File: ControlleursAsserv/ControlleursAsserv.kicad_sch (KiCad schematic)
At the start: 42 parts, among them J1 I2C1_5, J2 I2C2_5, J3 CAN1, J4 CAN2, J5 In App Prog, J6 DEBUG, SW1 RESET, SW2 BOOT0, U1 STM32G474RETx, U2 AMS1117-3.3, U3 MCP2558FD-xSN, Y1 16MHz

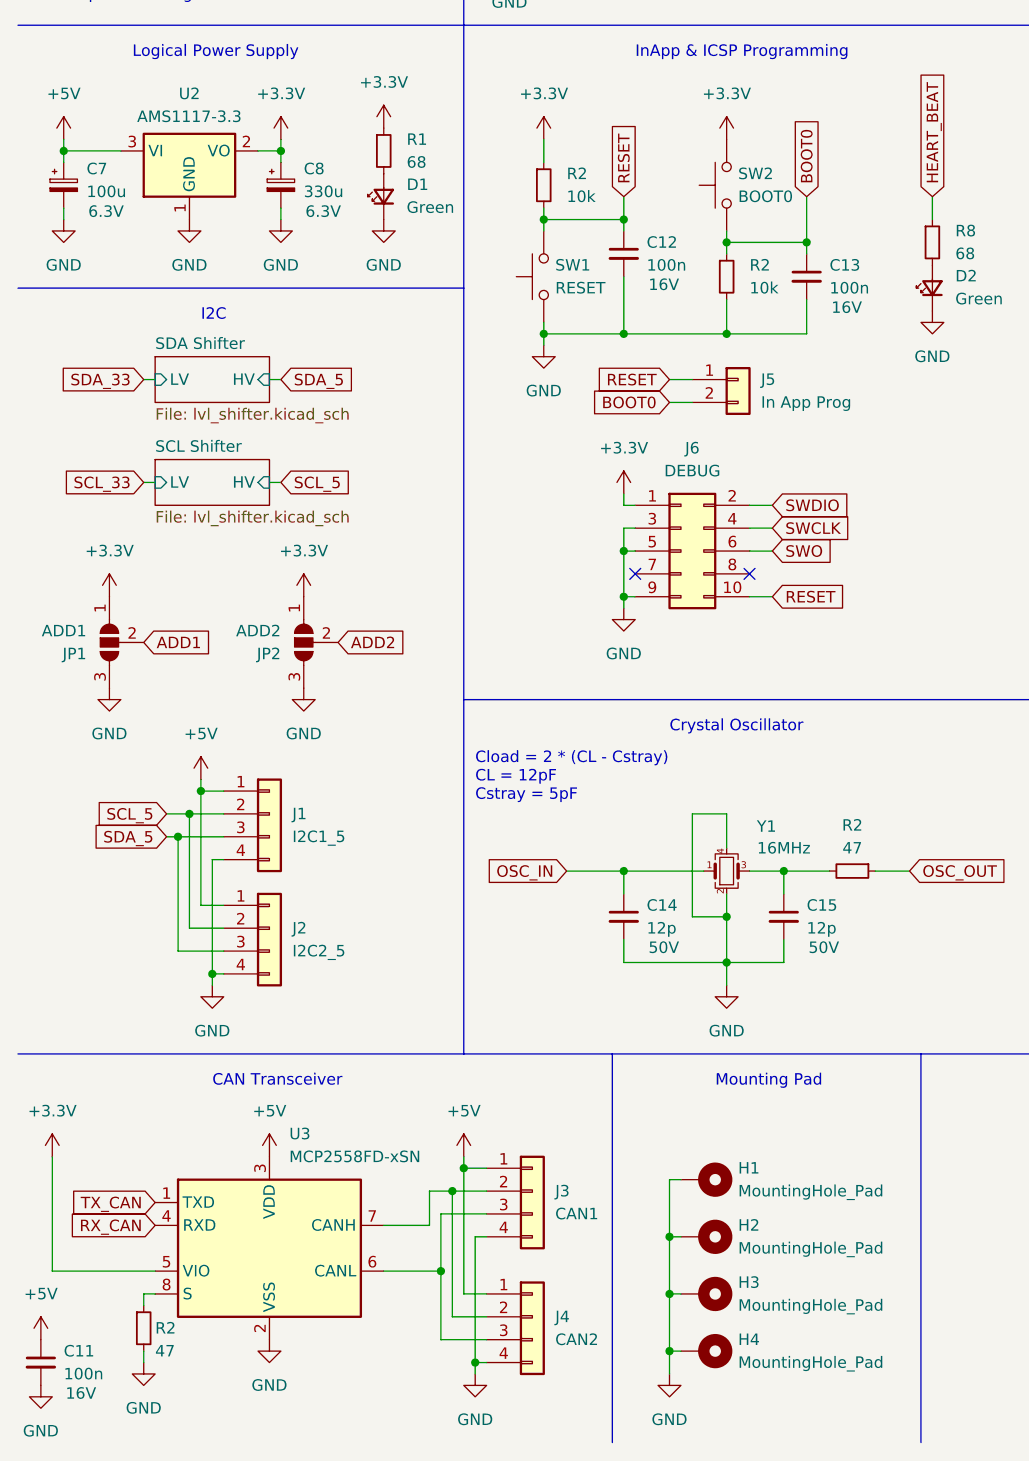
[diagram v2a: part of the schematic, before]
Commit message: Finalize placement for AsservController
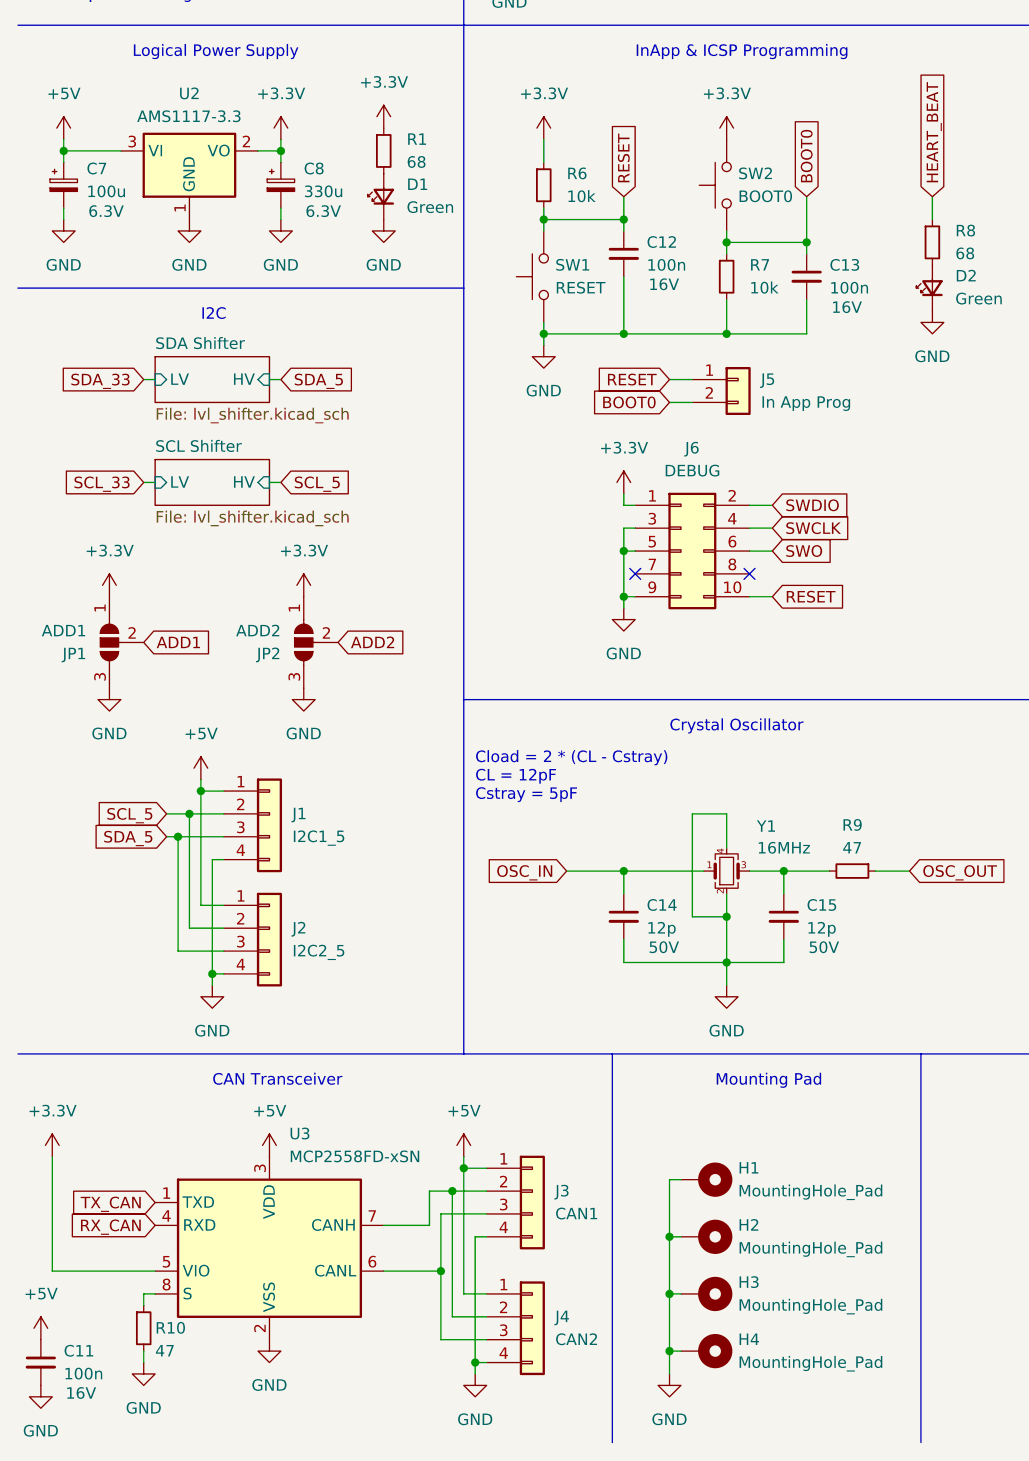
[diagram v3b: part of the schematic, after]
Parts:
- J1, J2, J3, J4: footprint Connector_JST:JST_EH_S4B-EH_1x04_P2.50mm_Horizontal -> Connector_JST:JST_PH_S4B-PH-K_1x04_P2.00mm_Horizontal
- J5: footprint Connector_JST:JST_EH_S2B-EH_1x02_P2.50mm_Horizontal -> Connector_JST:JST_PH_S2B-PH-K_1x02_P2.00mm_Horizontal
- renumbered R2 to R10, R2 to R6, R2 to R7, R2 to R9
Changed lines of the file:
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@@
       (effects (font (size 1.27 1.27)) (justify left))
     )
-    (property "Footprint" "Connector_JST:JST_EH_S4B-EH_1x04_P2.50mm_Horizontal" (at 69.85 168.91 0)
+    (property "Footprint" "Connector_JST:JST_PH_S4B-PH-K_1x04_P2.00mm_Horizontal" (at 69.85 168.91 0)
       (effects (font (size 1.27 1.27)) hide)
     )
@@
       (effects (font (size 1.27 1.27)) (justify left))
     )
-    (property "Footprint" "Connector_JST:JST_EH_S4B-EH_1x04_P2.50mm_Horizontal" (at 40.64 139.7 0)
+    (property "Footprint" "Connector_JST:JST_PH_S4B-PH-K_1x04_P2.00mm_Horizontal" (at 40.64 139.7 0)
       (effects (font (size 1.27 1.27)) hide)
     )
@@
       (effects (font (size 1.27 1.27)) (justify left))
     )
-    (property "Footprint" "Connector_JST:JST_EH_S4B-EH_1x04_P2.50mm_Horizontal" (at 69.85 182.88 0)
+    (property "Footprint" "Connector_JST:JST_PH_S4B-PH-K_1x04_P2.00mm_Horizontal" (at 69.85 182.88 0)
       (effects (font (size 1.27 1.27)) hide)
     )
@@
       (effects (font (size 1.27 1.27)) (justify left))
     )
-    (property "Footprint" "Connector_JST:JST_EH_S4B-EH_1x04_P2.50mm_Horizontal" (at 40.64 127 0)
+    (property "Footprint" "Connector_JST:JST_PH_S4B-PH-K_1x04_P2.00mm_Horizontal" (at 40.64 127 0)
       (effects (font (size 1.27 1.27)) hide)
     )
@@
   (symbol (lib_id "Device:R_Small") (at 91.44 67.31 0) (unit 1)
     (in_bom yes) (on_board yes) (dnp no) (fields_autoplaced)
-    (property "Reference" "R2" (at 93.98 66.04 0)
+    (property "Reference" "R7" (at 93.98 66.04 0)
       (effects (font (size 1.27 1.27)) (justify left))
     )
@@
     (instances
       (project "ControlleursAsserv"
-        (path "/c83bc042-587c-48f9-abdb-41233c8ec938/3da43f86-0520-4797-8d8a-f370cac20cce"
-          (reference "R2") (unit 1)
-        )
-        (path "/c83bc042-587c-48f9-abdb-41233c8ec938/089105fe-c96c-467a-9c54-c49136cd48fd"
-          (reference "R4") (unit 1)
-        )
         (path "/c83bc042-587c-48f9-abdb-41233c8ec938"
           (reference "R7") (unit 1)
@@
   (symbol (lib_id "Device:R_Small") (at 26.67 184.15 0) (unit 1)
     (in_bom yes) (on_board yes) (dnp no)
-    (property "Reference" "R2" (at 27.94 184.15 0)
+    (property "Reference" "R10" (at 27.94 184.15 0)
       (effects (font (size 1.27 1.27)) (justify left))
     )
@@
     (instances
       (project "ControlleursAsserv"
-        (path "/c83bc042-587c-48f9-abdb-41233c8ec938/3da43f86-0520-4797-8d8a-f370cac20cce"
-          (reference "R2") (unit 1)
-        )
-        (path "/c83bc042-587c-48f9-abdb-41233c8ec938/089105fe-c96c-467a-9c54-c49136cd48fd"
-          (reference "R4") (unit 1)
-        )
         (path "/c83bc042-587c-48f9-abdb-41233c8ec938"
           (reference "R10") (unit 1)
@@
   (symbol (lib_id "Device:R_Small") (at 71.12 57.15 0) (unit 1)
     (in_bom yes) (on_board yes) (dnp no) (fields_autoplaced)
-    (property "Reference" "R2" (at 73.66 55.88 0)
+    (property "Reference" "R6" (at 73.66 55.88 0)
       (effects (font (size 1.27 1.27)) (justify left))
     )
@@
     (instances
       (project "ControlleursAsserv"
-        (path "/c83bc042-587c-48f9-abdb-41233c8ec938/3da43f86-0520-4797-8d8a-f370cac20cce"
-          (reference "R2") (unit 1)
-        )
-        (path "/c83bc042-587c-48f9-abdb-41233c8ec938/089105fe-c96c-467a-9c54-c49136cd48fd"
-          (reference "R4") (unit 1)
-        )
         (path "/c83bc042-587c-48f9-abdb-41233c8ec938"
           (reference "R6") (unit 1)
@@
   (symbol (lib_id "Device:R_Small") (at 105.41 133.35 270) (unit 1)
     (in_bom yes) (on_board yes) (dnp no) (fields_autoplaced)
-    (property "Reference" "R2" (at 105.41 128.27 90)
+    (property "Reference" "R9" (at 105.41 128.27 90)
       (effects (font (size 1.27 1.27)))
     )
@@
     (instances
       (project "ControlleursAsserv"
-        (path "/c83bc042-587c-48f9-abdb-41233c8ec938/3da43f86-0520-4797-8d8a-f370cac20cce"
-          (reference "R2") (unit 1)
-        )
-        (path "/c83bc042-587c-48f9-abdb-41233c8ec938/089105fe-c96c-467a-9c54-c49136cd48fd"
-          (reference "R4") (unit 1)
-        )
         (path "/c83bc042-587c-48f9-abdb-41233c8ec938"
           (reference "R9") (unit 1)
@@
       (effects (font (size 1.27 1.27)) (justify left))
     )
-    (property "Footprint" "Connector_JST:JST_EH_S2B-EH_1x02_P2.50mm_Horizontal" (at 92.71 78.74 0)
-      (effects (font (size 1.27 1.27)) hide)
-    )
+    (property "Footprint" "Connector_JST:JST_PH_S2B-PH-K_1x02_P2.00mm_Horizontal" (at 92.71 78.74 0)
+      (effects (font (size 1.27 1.27)) hide)
+    )

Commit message: Init routing
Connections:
- net DIR_1: now also U1.4 (PC15); no longer U1.2 (PC13)
- net DIR_3: now also U1.2 (PC13); no longer U1.4 (PC15)
- net SLEEP_1: now also U1.22 (PC4); no longer U1.24 (PB0)
- net SLEEP_3: now also U1.24 (PB0); no longer U1.22 (PC4)
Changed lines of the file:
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@@
     )
   )
-  (global_label "SLEEP_3" (shape input) (at 213.36 83.82 180) (fields_autoplaced)
-    (effects (font (size 1.27 1.27)) (justify right))
-    (property "Intersheetrefs" "${INTERSHEET_REFS}" (at 202.3921 83.82 0)
-      (effects (font (size 1.27 1.27)) (justify right) hide)
+  (global_label "SLEEP_3" (shape input) (at 255.27 93.98 0) (fields_autoplaced)
+    (effects (font (size 1.27 1.27)) (justify left))
+    (property "Intersheetrefs" "${INTERSHEET_REFS}" (at 266.2379 93.98 0)
+      (effects (font (size 1.27 1.27)) (justify left) hide)
     )
   )
@@
     )
   )
-  (global_label "SLEEP_1" (shape input) (at 255.27 93.98 0) (fields_autoplaced)
-    (effects (font (size 1.27 1.27)) (justify left))
-    (property "Intersheetrefs" "${INTERSHEET_REFS}" (at 266.2379 93.98 0)
-      (effects (font (size 1.27 1.27)) (justify left) hide)
+  (global_label "SLEEP_1" (shape input) (at 213.36 83.82 180) (fields_autoplaced)
+    (effects (font (size 1.27 1.27)) (justify right))
+    (property "Intersheetrefs" "${INTERSHEET_REFS}" (at 202.3921 83.82 0)
+      (effects (font (size 1.27 1.27)) (justify right) hide)
     )
   )
@@
     )
   )
-  (global_label "DIR_3" (shape input) (at 213.36 111.76 180) (fields_autoplaced)
+  (global_label "DIR_3" (shape input) (at 213.36 106.68 180) (fields_autoplaced)
     (effects (font (size 1.27 1.27)) (justify right))
-    (property "Intersheetrefs" "${INTERSHEET_REFS}" (at 205.0529 111.76 0)
+    (property "Intersheetrefs" "${INTERSHEET_REFS}" (at 205.0529 106.68 0)
       (effects (font (size 1.27 1.27)) (justify right) hide)
     )
@@
     )
   )
-  (global_label "DIR_1" (shape input) (at 213.36 106.68 180) (fields_autoplaced)
+  (global_label "DIR_1" (shape input) (at 213.36 111.76 180) (fields_autoplaced)
     (effects (font (size 1.27 1.27)) (justify right))
-    (property "Intersheetrefs" "${INTERSHEET_REFS}" (at 205.0529 106.68 0)
+    (property "Intersheetrefs" "${INTERSHEET_REFS}" (at 205.0529 111.76 0)
       (effects (font (size 1.27 1.27)) (justify right) hide)
     )

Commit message: Finish Controller Asserv
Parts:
- added C16: 100n, Capacitor_SMD:C_0402_1005Metric_Pad0.74x0.62mm_HandSolder, symbol Device:C_Small
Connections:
- net +3.3V: now also C16.1
- net GND: now also C16.2
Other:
- moved on the sheet: C11
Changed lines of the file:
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@@
   (junction (at 41.91 53.34) (diameter 0) (color 0 0 0 0)
+  )
+  (junction (at 16.51 177.8) (diameter 0) (color 0 0 0 0)
   )
   (junction (at 33.02 124.46) (diameter 0) (color 0 0 0 0)
@@
     (stroke (width 0) (type default))
   )
+  (wire (pts (xy 16.51 177.8) (xy 16.51 181.61))
+    (stroke (width 0) (type default))
+  )
   (wire (pts (xy 87.63 21.59) (xy 77.47 21.59))
     (stroke (width 0) (type default))
@@
   )
   (wire (pts (xy 64.77 171.45) (xy 59.69 171.45))
+    (stroke (width 0) (type default))
+  )
+  (wire (pts (xy 16.51 186.69) (xy 16.51 187.96))
     (stroke (width 0) (type default))
   )
@@
     )
   )
-  (symbol (lib_id "power:+5V") (at 15.24 185.42 0) (unit 1)
-    (in_bom yes) (on_board yes) (dnp no) (fields_autoplaced)
-    (property "Reference" "#PWR033" (at 15.24 189.23 0)
-      (effects (font (size 1.27 1.27)) hide)
-    )
-    (property "Value" "+5V" (at 15.24 180.34 0)
-      (effects (font (size 1.27 1.27)))
-    )
-    (property "Footprint" "" (at 15.24 185.42 0)
-      (effects (font (size 1.27 1.27)) hide)
-    )
-    (property "Datasheet" "" (at 15.24 185.42 0)
+  (symbol (lib_id "power:+5V") (at 53.34 185.42 0) (unit 1)
+    (in_bom yes) (on_board yes) (dnp no) (fields_autoplaced)
+    (property "Reference" "#PWR033" (at 53.34 189.23 0)
+      (effects (font (size 1.27 1.27)) hide)
+    )
+    (property "Value" "+5V" (at 53.34 180.34 0)
+      (effects (font (size 1.27 1.27)))
+    )
+    (property "Footprint" "" (at 53.34 185.42 0)
+      (effects (font (size 1.27 1.27)) hide)
+    )
+    (property "Datasheet" "" (at 53.34 185.42 0)
       (effects (font (size 1.27 1.27)) hide)
     )
@@
     )
   )
-  (symbol (lib_id "power:GND") (at 15.24 190.5 0) (unit 1)
-    (in_bom yes) (on_board yes) (dnp no) (fields_autoplaced)
-    (property "Reference" "#PWR034" (at 15.24 196.85 0)
-      (effects (font (size 1.27 1.27)) hide)
-    )
-    (property "Value" "GND" (at 15.24 195.58 0)
-      (effects (font (size 1.27 1.27)))
-    )
-    (property "Footprint" "" (at 15.24 190.5 0)
-      (effects (font (size 1.27 1.27)) hide)
-    )
-    (property "Datasheet" "" (at 15.24 190.5 0)
+  (symbol (lib_id "power:GND") (at 53.34 190.5 0) (unit 1)
+    (in_bom yes) (on_board yes) (dnp no) (fields_autoplaced)
+    (property "Reference" "#PWR034" (at 53.34 196.85 0)
+      (effects (font (size 1.27 1.27)) hide)
+    )
+    (property "Value" "GND" (at 53.34 195.58 0)
+      (effects (font (size 1.27 1.27)))
+    )
+    (property "Footprint" "" (at 53.34 190.5 0)
+      (effects (font (size 1.27 1.27)) hide)
+    )
+    (property "Datasheet" "" (at 53.34 190.5 0)
       (effects (font (size 1.27 1.27)) hide)
     )
@@
     )
   )
-  (symbol (lib_id "Device:C_Small") (at 15.24 187.96 0) (unit 1)
+  (symbol (lib_id "Device:C_Small") (at 53.34 187.96 0) (unit 1)
     (in_bom yes) (on_board yes) (dnp no)
-    (property "Reference" "C11" (at 17.78 186.6963 0)
-      (effects (font (size 1.27 1.27)) (justify left))
-    )
-    (property "Value" "100n" (at 17.78 189.2363 0)
-      (effects (font (size 1.27 1.27)) (justify left))
-    )
-    (property "Footprint" "Capacitor_SMD:C_0402_1005Metric_Pad0.74x0.62mm_HandSolder" (at 15.24 187.96 0)
-      (effects (font (size 1.27 1.27)) hide)
-    )
-    (property "Datasheet" "~" (at 15.24 187.96 0)
-      (effects (font (size 1.27 1.27)) hide)
-    )
-    (property "JLCPCB BOM" "" (at 15.24 187.96 0)
-      (effects (font (size 1.27 1.27)) hide)
-    )
-    (property "LCSC Part" "C1525" (at 15.24 187.96 0)
-      (effects (font (size 1.27 1.27)) hide)
-    )
-    (property "Tension" "16V" (at 19.685 191.389 0)
+    (property "Reference" "C11" (at 55.88 186.6963 0)
+      (effects (font (size 1.27 1.27)) (justify left))
+    )
+    (property "Value" "100n" (at 55.88 189.2363 0)
+      (effects (font (size 1.27 1.27)) (justify left))
+    )
+    (property "Footprint" "Capacitor_SMD:C_0402_1005Metric_Pad0.74x0.62mm_HandSolder" (at 53.34 187.96 0)
+      (effects (font (size 1.27 1.27)) hide)
+    )
+    (property "Datasheet" "~" (at 53.34 187.96 0)
+      (effects (font (size 1.27 1.27)) hide)
+    )
+    (property "JLCPCB BOM" "" (at 53.34 187.96 0)
+      (effects (font (size 1.27 1.27)) hide)
+    )
+    (property "LCSC Part" "C1525" (at 53.34 187.96 0)
+      (effects (font (size 1.27 1.27)) hide)
+    )
+    (property "Tension" "16V" (at 57.785 191.389 0)
       (effects (font (size 1.27 1.27)))
     )
@@
     )
   )
+  (symbol (lib_id "Device:C_Small") (at 16.51 184.15 0) (unit 1)
+    (in_bom yes) (on_board yes) (dnp no)
+    (property "Reference" "C16" (at 19.05 182.8863 0)
+      (effects (font (size 1.27 1.27)) (justify left))
+    )
+    (property "Value" "100n" (at 19.05 185.4263 0)
+      (effects (font (size 1.27 1.27)) (justify left))
+    )
+    (property "Footprint" "Capacitor_SMD:C_0402_1005Metric_Pad0.74x0.62mm_HandSolder" (at 16.51 184.15 0)
+      (effects (font (size 1.27 1.27)) hide)
+    )
+    (property "Datasheet" "~" (at 16.51 184.15 0)
+      (effects (font (size 1.27 1.27)) hide)
+    )
+    (property "JLCPCB BOM" "" (at 16.51 184.15 0)
+      (effects (font (size 1.27 1.27)) hide)
+    )
+    (property "LCSC Part" "C1525" (at 16.51 184.15 0)
+      (effects (font (size 1.27 1.27)) hide)
+    )
+    (property "Tension" "16V" (at 20.955 187.579 0)
+      (effects (font (size 1.27 1.27)))
+    )
+    (pin "1")
+    (pin "2")
+    (instances
+      (project "ControlleursAsserv"
+        (path "/c83bc042-587c-48f9-abdb-41233c8ec938"
+          (reference "C16") (unit 1)
+        )
+      )
+    )
+  )
   (symbol (lib_id "power:GND") (at 41.91 60.96 0) (unit 1)
     (in_bom yes) (on_board yes) (dnp no) (fields_autoplaced)
@@
         )
       )
+    )
+  )
+  (symbol (lib_id "power:GND") (at 16.51 187.96 0) (unit 1)
+    (in_bom yes) (on_board yes) (dnp no) (fields_autoplaced)
+    (property "Reference" "#PWR060" (at 16.51 194.31 0)
+      (effects (font (size 1.27 1.27)) hide)
+    )
+    (property "Value" "GND" (at 16.51 193.04 0)
+      (effects (font (size 1.27 1.27)))
+    )
+    (property "Footprint" "" (at 16.51 187.96 0)
+      (effects (font (size 1.27 1.27)) hide)
+    )
+    (property "Datasheet" "" (at 16.51 187.96 0)
+      (effects (font (size 1.27 1.27)) hide)
+    )
+    (pin "1")
+    (instances
+      (project "ControlleursAsserv"
+        (path "/c83bc042-587c-48f9-abdb-41233c8ec938"
+          (reference "#PWR060") (unit 1)
+        )
+      )

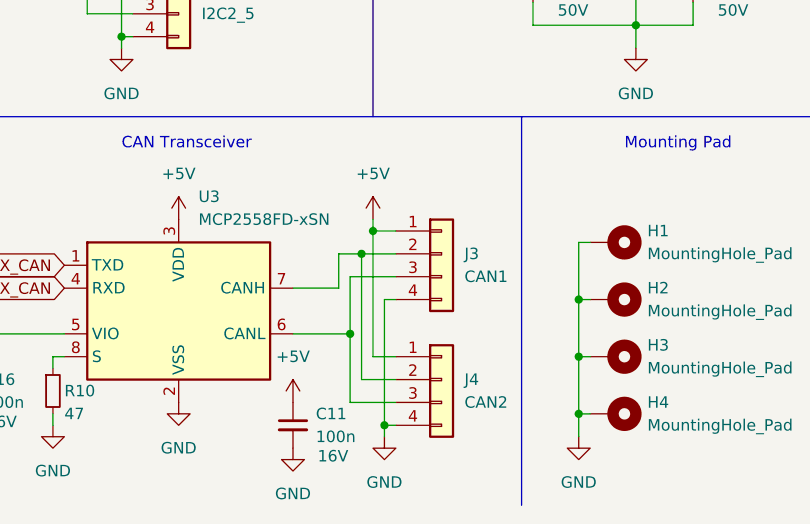
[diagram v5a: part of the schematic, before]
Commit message: Fix CAN connections to improve routing on ControllerAsserv
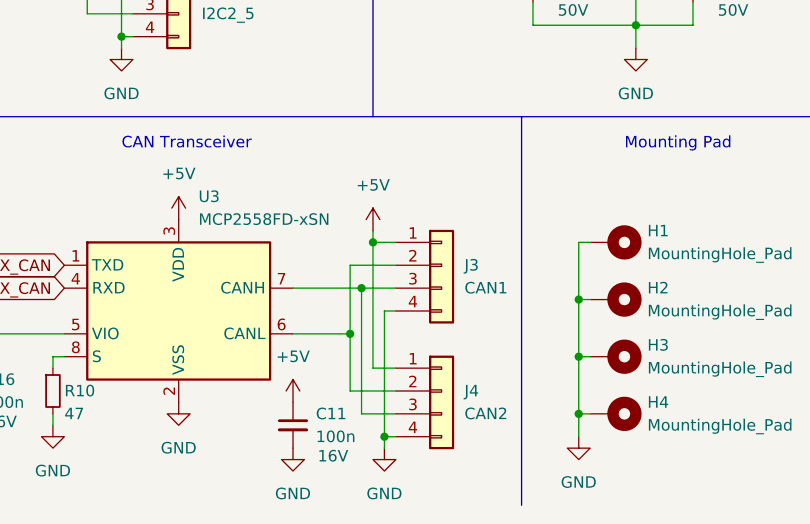
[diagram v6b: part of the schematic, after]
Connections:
- net at J3.3 (Pin_3), J4.3 (Pin_3): now also U3.7 (CANH); no longer U3.6 (CANL)
- net at J3.2 (Pin_2), J4.2 (Pin_2): now also U3.6 (CANL); no longer U3.7 (CANH)
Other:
- moved on the sheet: J3, J4
